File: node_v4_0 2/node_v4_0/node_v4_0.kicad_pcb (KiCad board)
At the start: 4 copper layers, 45.7 x 76.2 mm, 90 parts, among them J1 Conn_01x02_Pin, J2 12402012E212A, J3 Conn_Coaxial, J4 Conn_02x08_Odd_Even, J5 Conn_02x02_Odd_Even, J6 GNSS_ANT, J7 RF_ANT, Q1 DMG2301L, U1 RP2040, U10 MCP7940N-xP, U11 1042240820, U12 CAT24M01W, U13 MAX31342EWA+T, U2 W25Q128JVS, U3 AP2112K-3.3, U4 CAT3200-5, U5 MCP73831-2-OT, U6 RFM69HCW, U7 PTS526 SK15 SMTR2 LFS, U8 PTS526 SK15 SMTR2 LFS, U9 SIM7080G

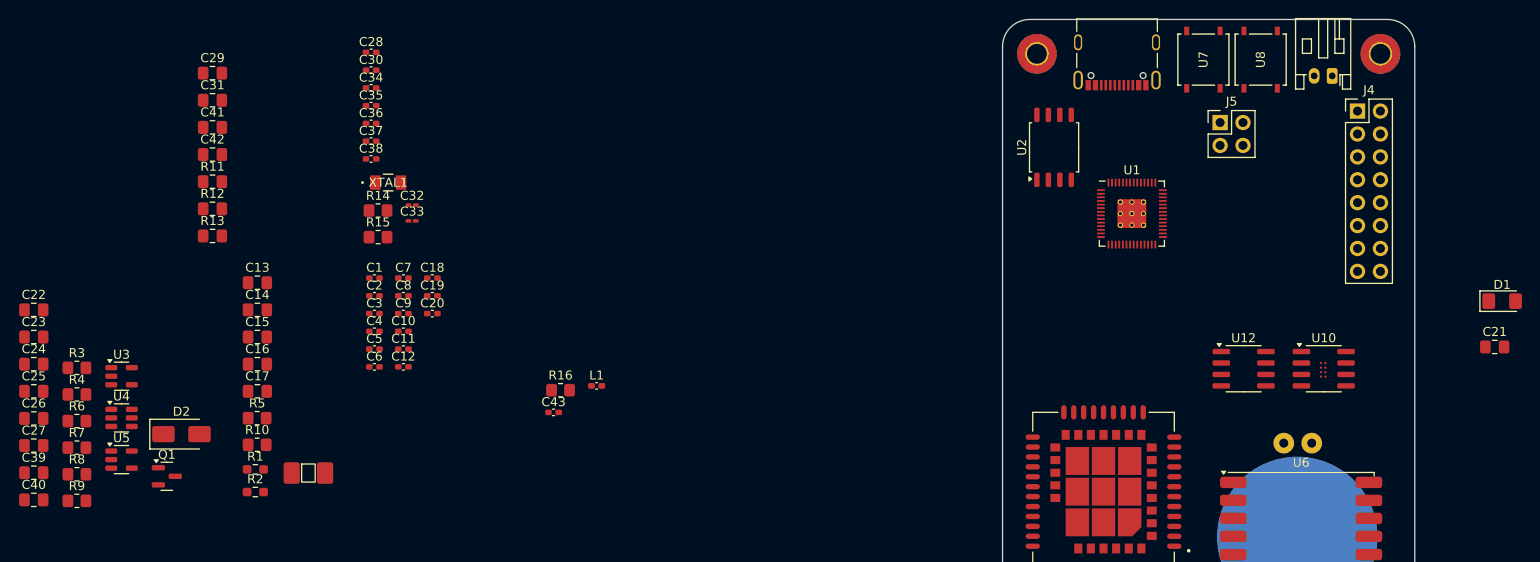
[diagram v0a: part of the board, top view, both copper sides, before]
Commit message: placed power supplies
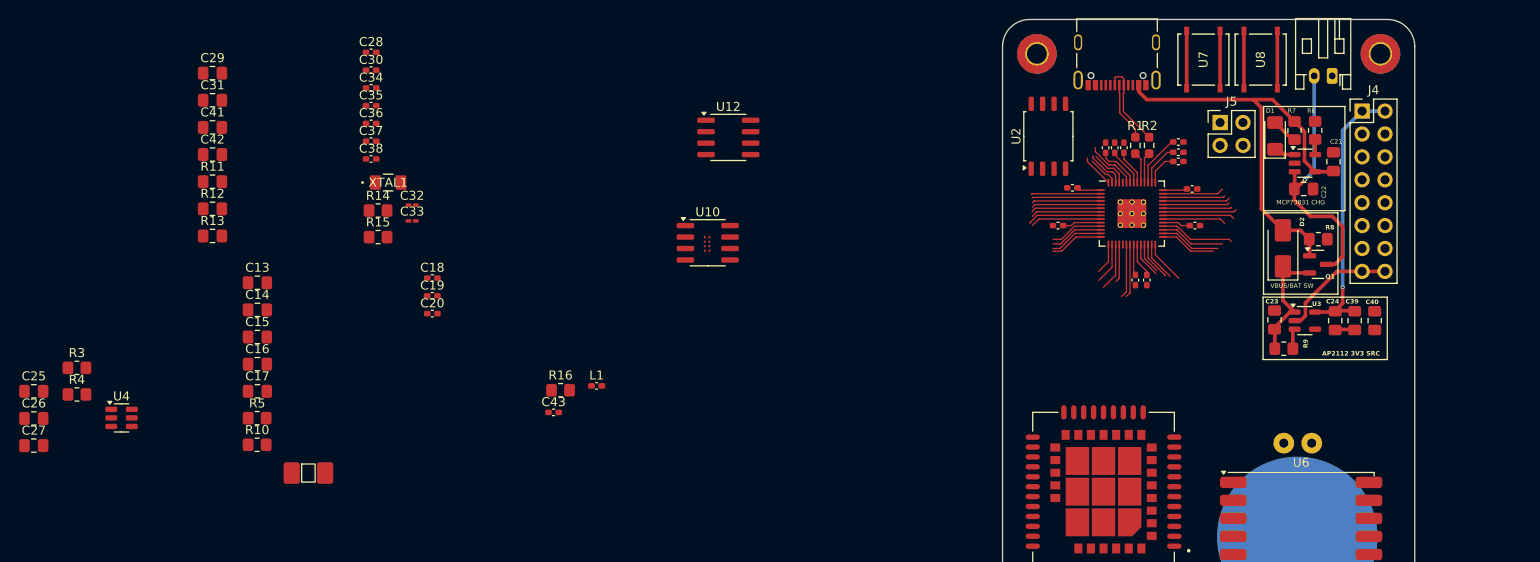
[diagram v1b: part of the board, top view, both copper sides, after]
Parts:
- moved C40 150.0 mm to (244.5, 84.2), turned to 90 degrees
- moved C39 147.5 mm to (242.3, 84.2), turned to -90 degrees
- moved C24 144.4 mm to (240.1, 84.2), turned to -90 degrees
- moved C22 141.5 mm to (236.6, 69.6)
- moved R6 141.1 mm to (237.9, 63.1), turned to 90 degrees
- moved R8 140.1 mm to (238.2, 75.2)
- moved R7 139.6 mm to (235.6, 63.1), turned to 90 degrees
- moved C23 137.6 mm to (233.4, 84.1), turned to 90 degrees
- moved U5 135.3 mm to (236.7, 66.7)
- moved R9 134.9 mm to (234.4, 87.3)
- moved U3 131.4 mm to (236.7, 84.2)
- moved Q1 129.8 mm to (238.2, 78.0)
- moved D2 123.9 mm to (234.3, 76.2), turned to 90 degrees
- moved R2 106.3 mm to (219.5, 64.8), turned to 90 degrees
- moved R1 104.0 mm to (217.9, 64.8), turned to 90 degrees
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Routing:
- net +3.3V: track 0.00 -> 63.3 mm, vias 0 -> 1
- net VBUS: track 0.00 -> 49.0 mm
- net +BATT: track 0.00 -> 28.7 mm, vias 0 -> 1
- net GND: track 0.00 -> 21.6 mm
- net +1V1: track 0.00 -> 14.4 mm
- net +VSW: track 0.00 -> 14.1 mm
- net /MCU/RESET: track 0.00 -> 10.6 mm
- net /MCU/CS: track 0.00 -> 10.1 mm
- net USB-: track 0.00 -> 9.61 mm
- net SPI_CS: track 0.00 -> 8.33 mm
- net GP6: track 0.00 -> 8.27 mm
- net unconnected-(U1-GPIO24-Pad36): track 0.00 -> 8.23 mm
- net unconnected-(U1-GPIO23-Pad35): track 0.00 -> 8.03 mm
- net GP7: track 0.00 -> 7.91 mm
- net SDA: track 0.00 -> 7.82 mm
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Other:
- board text added: "AP2112 3V3 SRC"
- board text added: "C21"
- board text added: "C22"
- board text added: "C23"
- board text added: "C24"
- board text added: "C39"
- board text added: "C40"
- board text added: "D1"
- board text added: "D2"
- board text added: "MCP73831 CHG"
- board text added: "Q1"
- board text added: "R6"
- board text added: "R7"
- board text added: "R8"
- board text added: "R9"
- board text added: "U3"
- board text added: "VBUS/BAT SW"

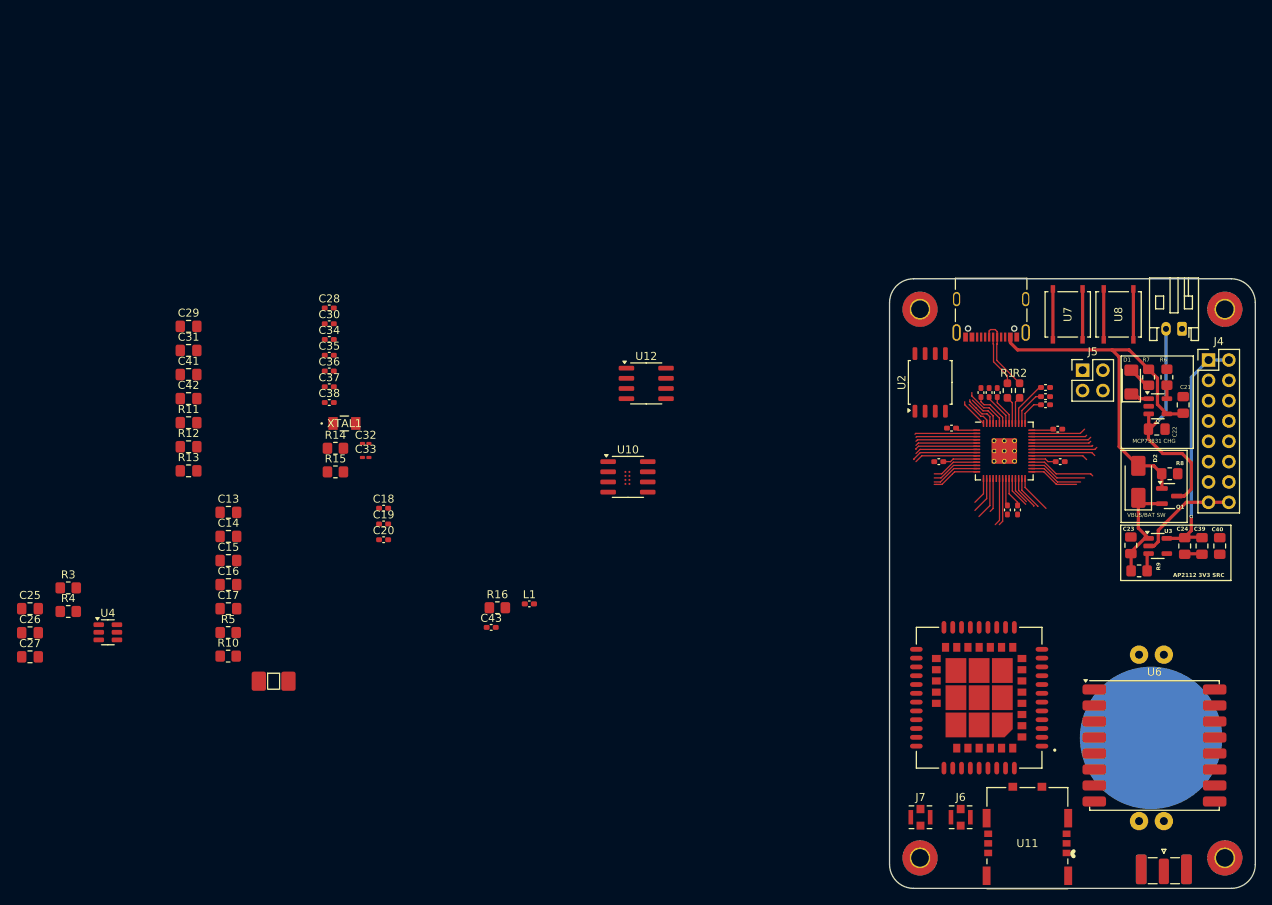
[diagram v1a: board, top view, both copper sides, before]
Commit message: finished laying out the board
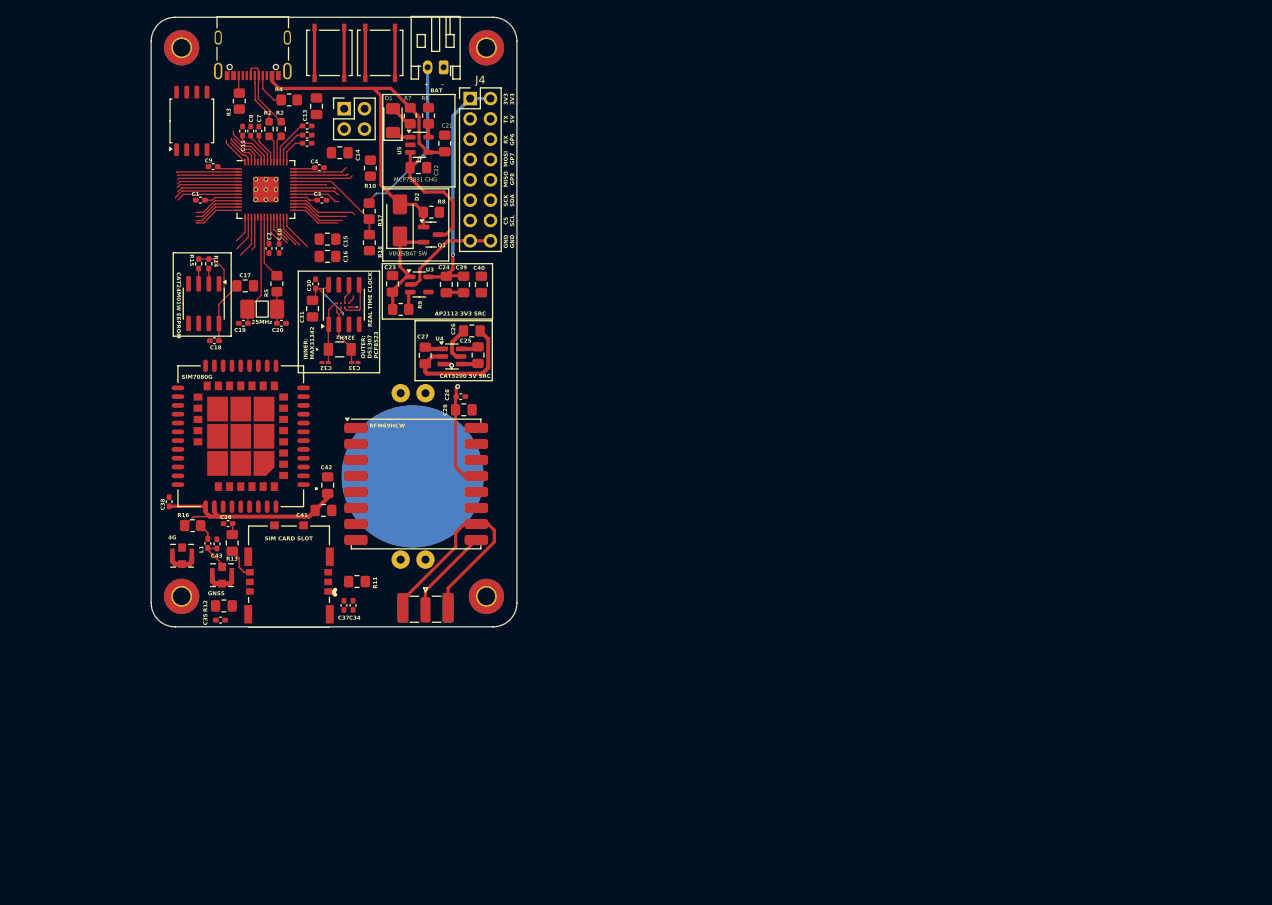
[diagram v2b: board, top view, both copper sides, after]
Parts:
- added R17: 470k, Resistor_SMD:R_0805_2012Metric_Pad1.20x1.40mm_HandSolder, F.Cu at (138.2, 42.3)
- added R18: 470k, Resistor_SMD:R_0805_2012Metric_Pad1.20x1.40mm_HandSolder, F.Cu at (138.2, 46.3)
- J2: footprint usbc:AMPHENOL_12402012E212A -> WiSDOM:AMPHENOL_12402012E212A
- R14, R15: footprint Resistor_SMD:R_0805_2012Metric_Pad1.20x1.40mm_HandSolder -> Resistor_SMD:R_0402_1005Metric_Pad0.72x0.64mm_HandSolder
- U10: value MCP7940N-xP -> MCP7940 / DS1307 / PCF8523
- U7, U8: footprint pts526:SMT_FS -> WiSDOM:PTS526
- moved J2 97.9 mm to (123.6, 20.7)
- moved U9 97.9 mm to (122.1, 70.5)
- moved H2 97.9 mm to (152.8, 21.9)
- moved H3 97.9 mm to (152.8, 90.5)
- moved J5 97.9 mm to (135.0, 29.5)
- moved C1 97.9 mm to (117.1, 41.0)
- moved C10 97.9 mm to (126.9, 47.0)
- moved C11 97.9 mm to (122.3, 32.3)
- moved C21 97.9 mm to (147.6, 33.9)
- moved C22 97.9 mm to (144.3, 36.9)
- moved C23 97.9 mm to (141.1, 51.4)
- moved C3 97.9 mm to (132.2, 41.0)
- moved C4 97.9 mm to (131.9, 36.9)
- moved C5 97.9 mm to (130.4, 33.9)
- moved C6 97.9 mm to (130.4, 32.8)
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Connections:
- C32 pad 1: Net-(U10-X1) -> /PERIPHERALS/RTC_X1
- C33 pad 1: Net-(U10-X2) -> /PERIPHERALS/RTC_X2
- U1 pad 38: unconnected-(U1-GPIO26_ADC0-Pad38) -> VBAT_SAMPLE
- U1 pad 4: unconnected-(U1-GPIO2-Pad4) -> RTC_MFP1
- U1 pad 5: RTC_MFP -> RTC_MFP2
- U10 pad 1: Net-(U10-X1) -> /PERIPHERALS/RTC_X1
- U10 pad 2: Net-(U10-X2) -> /PERIPHERALS/RTC_X2
- U10 pad 7: RTC_MFP -> RTC_MFP1
- U13 pad A1: unconnected-(U13-X2-PadA1) -> /PERIPHERALS/RTC_X1
- U13 pad A2: unconnected-(U13-GND-PadA2) -> GND
- U13 pad A3: unconnected-(U13-SCL-PadA3) -> SCL
- U13 pad A4: unconnected-(U13-*INTB/CLKOUT-PadA4) -> RTC_MFP2
- U13 pad B1: unconnected-(U13-X1-PadB1) -> /PERIPHERALS/RTC_X2
- U13 pad B2: unconnected-(U13-VCC-PadB2) -> +3.3V
- U13 pad B3: unconnected-(U13-SDA-PadB3) -> SDA
- U13 pad B4: unconnected-(U13-*INTA/CLKIN-PadB4) -> RTC_MFP1
- XTAL1 pad 1: Net-(U10-X1) -> /PERIPHERALS/RTC_X1
- XTAL1 pad 2: Net-(U10-X2) -> /PERIPHERALS/RTC_X2
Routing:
- net +3.3V: track 63.3 -> 129.0 mm, vias 1 -> 4
- net GND: track 21.6 -> 76.7 mm
- net VBAT_SAMPLE: track 0.00 -> 13.4 mm
- net /PERIPHERALS/ANT: track 0.00 -> 11.4 mm
- net RTC_MFP2: track 0.00 -> 8.87 mm
- net RTC_MFP1: track 0.00 -> 8.71 mm, vias 0 -> 1
- net +BATT: track 28.7 -> 37.4 mm, vias 1 -> 2
- net /MCU/XTAL+: track 5.99 -> 14.0 mm
- net /PERIPHERALS/RTC_X1: track 0.00 -> 7.98 mm
- net RTC_MFP: track 7.73 -> 0.00 mm
- net /PERIPHERALS/RTC_X2: track 0.00 -> 7.69 mm
- net unconnected-(U1-GPIO2-Pad4): track 7.68 -> 0.00 mm
- net unconnected-(U1-GPIO26_ADC0-Pad38): track 7.45 -> 0.00 mm
- net SDA: track 7.82 -> 13.1 mm
- net +VSW: track 14.1 -> 18.7 mm
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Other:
- board text added: "+"
- board text added: "-"
- board text added: "25MHz"
- board text added: "32kHz"
- board text added: "3V3 3V3"
- board text added: "4G"
- board text added: "BAT"
- board text added: "C1"
- board text added: "C10"
- board text added: "C11"
- board text added: "C13"
- board text added: "C14"
- board text added: "C15"
- board text added: "C16"
- board text added: "C17"
- board text added: "C18"
- board text added: "C19"
- board text added: "C2"
- board text added: "C20"
- board text added: "C25"
- board text added: "C26"
- board text added: "C27"
- board text added: "C28"
- board text added: "C29"
- board text added: "C3"
- board text added: "C30"
- board text added: "C31"
- board text added: "C32"
- board text added: "C33"
- board text added: "C34"
- board text added: "C35"
- board text added: "C36"
- board text added: "C37"
- board text added: "C38"
- board text added: "C4"
- board text added: "C41"
- board text added: "C42"
- board text added: "C43"
- board text added: "C7"
- board text added: "C8"
- board text added: "C9"
- board text added: "CAT24M01W EEPROM"
- board text added: "CAT3200 5V SRC"
- board text added: "CS SCL"
- board text added: "GND GND"
- board text added: "GNSS"
- board text added: "INNER: MAX31342"
- board text added: "L1"
- board text added: "MISO GP8"
- board text added: "MOSI GP7"
- board text added: "OUTER: DS1307 PCF8523"
- board text added: "R1"
- board text added: "R10"
- board text added: "R11"
- board text added: "R12"
- board text added: "R13"
- board text added: "R14"
- board text added: "R15"
- board text added: "R16"
- board text added: "R17"
- board text added: "R18"
- board text added: "R2"
- board text added: "R3"
- board text added: "R4"
- board text added: "R5"
- board text added: "REAL TIME CLOCK"
- board text added: "RFM69HCW"
- board text added: "RX GP6"
- board text added: "SCK SDA"
- board text added: "SIM CARD SLOT"
- board text added: "SIM7080G"
- board text added: "TX 5V"
- board text added: "U4"
- board text added: "U5"

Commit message: most routing done
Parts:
- added C44: 0.1u, Capacitor_SMD:C_0402_1005Metric_Pad0.74x0.62mm_HandSolder, F.Cu at (119.9, 59.2)
- added C45: 10u, Capacitor_SMD:C_0805_2012Metric_Pad1.18x1.45mm_HandSolder, F.Cu at (119.1, 46.4)
- added C46: 10u, Capacitor_SMD:C_0805_2012Metric_Pad1.18x1.45mm_HandSolder, F.Cu at (138.8, 53.2)
- added D3: SS14, Diode_SMD:D_SMA, F.Cu at (140.4, 61.8)
- added Q2: DMG2301L, Package_TO_SOT_SMD:SOT-23, F.Cu at (141.6, 57.9)
- added R19: 100k, Resistor_SMD:R_0805_2012Metric_Pad1.20x1.40mm_HandSolder, F.Cu at (132.8, 65.7)
- BT1: value Battery_Cell -> RTC_BAT
- moved C18 33.1 mm to (117.0, 25.5), turned to 0 degrees
- moved C17 23.3 mm to (119.9, 28.6), turned to -90 degrees
- moved C33 0.82 mm to (135.5, 61.2), turned to 180 degrees
- moved C32 0.81 mm to (133.5, 61.2), turned to 0 degrees
- moved C14 0.55 mm to (134.0, 35.3)
- moved BT1 0.13 mm to (143.5, 75.4)
- turned R11 to 180 degrees
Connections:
- net Net-(BT1-+) renamed RTC_BAT
- J4 pad 10: GP8 -> GP29
- J4 pad 6: GP6 -> GP27
- J4 pad 8: GP7 -> GP28
- U1 pad 11: GP8 -> unconnected-(U1-GPIO8-Pad11)
- U1 pad 39: unconnected-(U1-GPIO27_ADC1-Pad39) -> GP27
- U1 pad 40: unconnected-(U1-GPIO28_ADC2-Pad40) -> GP28
- U1 pad 41: unconnected-(U1-GPIO29_ADC3-Pad41) -> GP29
- U1 pad 8: GP6 -> unconnected-(U1-GPIO6-Pad8)
- U1 pad 9: GP7 -> unconnected-(U1-GPIO7-Pad9)
- U13 pad B2: +3.3V -> +VRTC
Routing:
- net +3.3V: track 129.0 -> 347.8 mm, vias 4 -> 11
- net GND: track 76.7 -> 231.8 mm, vias 0 -> 4
- net RX1: track 7.64 -> 92.5 mm, vias 0 -> 3
- net TX1: track 7.77 -> 91.5 mm, vias 0 -> 4
- net SDA: track 13.1 -> 86.4 mm, vias 0 -> 3
- net SCL: track 10.3 -> 80.9 mm, vias 0 -> 3
- net SPI_CK: track 6.24 -> 61.3 mm, vias 0 -> 3
- net MISO: track 4.31 -> 59.1 mm, vias 0 -> 3
- net MOSI: track 6.79 -> 61.5 mm, vias 0 -> 4
- net RTC_BAT: track 0.00 -> 43.2 mm, vias 0 -> 2
- net RFM_RST: track 7.25 -> 47.9 mm, vias 0 -> 4
- net /PERIPHERALS/SIM_RST: track 0.00 -> 39.0 mm, vias 0 -> 2
- net /PERIPHERALS/SIM_VCC: track 0.00 -> 37.3 mm, vias 0 -> 2
- net /PERIPHERALS/SIM_CLK: track 0.00 -> 36.7 mm, vias 0 -> 2
- net RFM_CS: track 4.82 -> 40.8 mm, vias 0 -> 3
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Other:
- board text added: "3V3"
- board text added: "C45"
- board text added: "C47"
- board text added: "CR2032"
- board text added: "D3"
- board text added: "GND"
- board text added: "MISO GP29"
- board text added: "MOSI GP28"
- board text added: "Q2"
- board text added: "R19"
- board text added: "RP2040"
- board text added: "RTC BACKUP"
- board text added: "RX GP27"
- board text added: "SWCLK"
- board text added: "SWD"
- board text added: "W25Q128"
- board text removed: "MISO GP8"
- board text removed: "MOSI GP7"
- board text removed: "RX GP6"

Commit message: done!
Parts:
- moved C35 1.23 mm to (118.4, 93.2), turned to 180 degrees
- moved C36 0.51 mm to (121.0, 81.4), turned to 0 degrees
- moved C4 0.13 mm to (131.8, 36.8)
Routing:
- net GND: track 231.8 -> 286.1 mm, vias 4 -> 6
- net +1V1: track 22.3 -> 35.7 mm, vias 0 -> 3
- net +3.3V: track 347.8 -> 343.1 mm, vias 11 -> 14
- net SCL: track 80.9 -> 77.3 mm, vias 3 -> 4
- net /PERIPHERALS/SIM_RST: track 39.0 -> 42.1 mm
- net TX1: track 91.5 -> 93.9 mm
- net SDA: track 86.4 -> 84.2 mm, vias 3 -> 5
- net SIM_DTR: track 35.2 -> 33.6 mm
- net RX1: track 92.5 -> 93.8 mm
- net +VSW: track 28.7 -> 29.2 mm, vias 0 -> 2
- net VBAT_SAMPLE: track 13.4 -> 13.7 mm, vias 0 -> 2
- net VBUS: track 55.6 -> 55.9 mm, vias 0 -> 2
- net RFM_RST: track 47.9 -> 48.2 mm, vias 4 -> 3
- net /MCU/CS: vias 2 -> 3
- added copper zone on B.Cu, net GND
- added copper zone on F.Cu, net GND
